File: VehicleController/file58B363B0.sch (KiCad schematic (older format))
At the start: 10 parts, among them P3 CONN_01X02, P4 MX150_8, U11 NDC7002N, U12 MCP2551

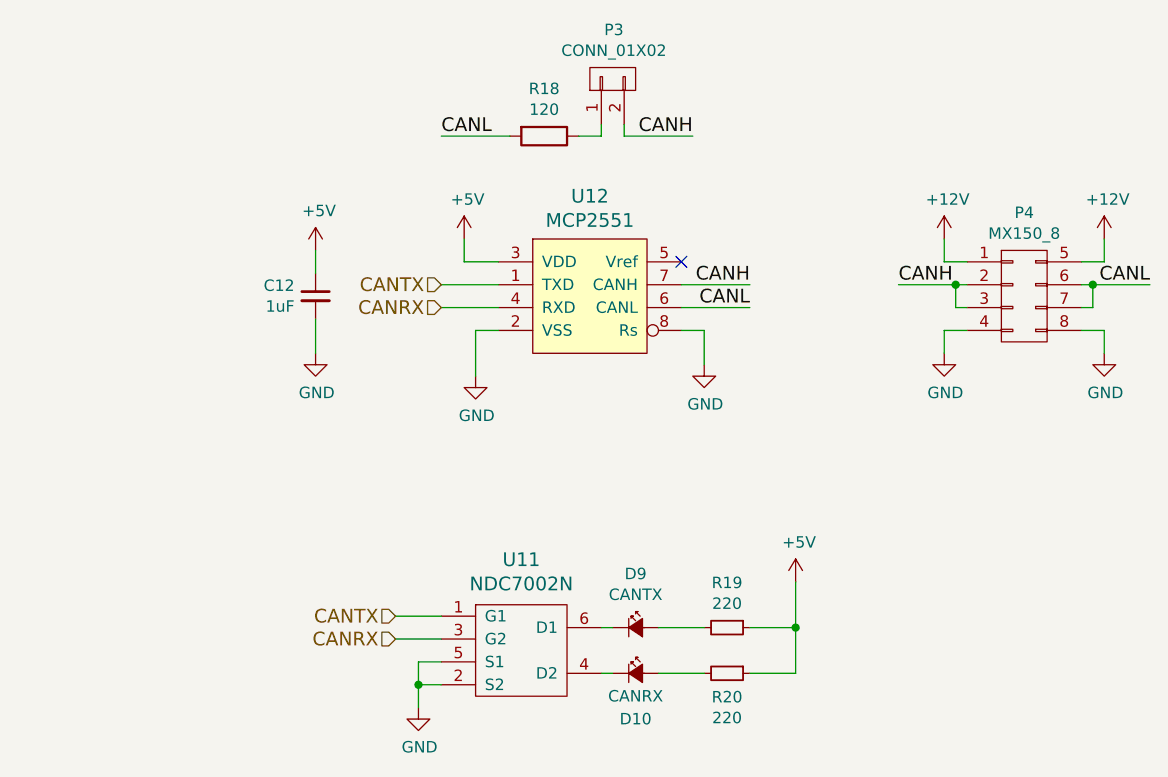
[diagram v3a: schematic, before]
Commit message: Add BTS4130's for 12v and 5v outputs
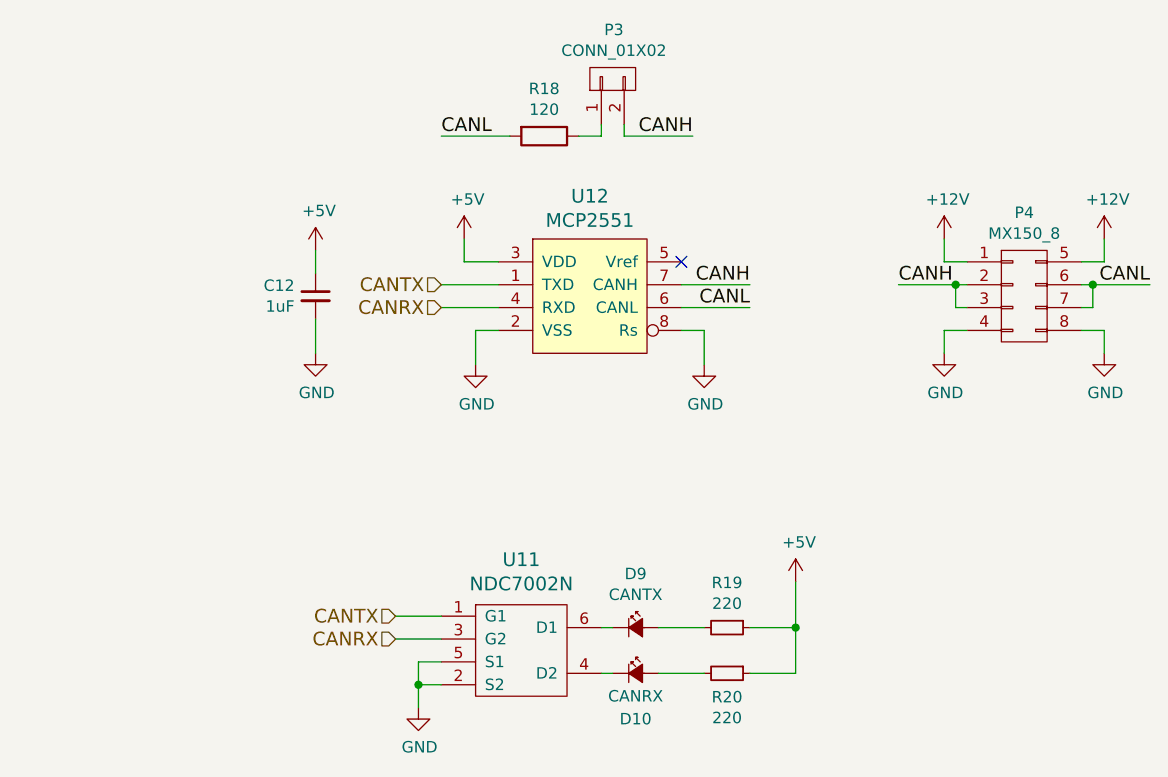
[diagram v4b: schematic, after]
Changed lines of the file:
@@
 L GND #PWR52
 U 1 1 58B3659A
-P 4950 3550
-F 0 "#PWR52" H 4950 3300 50  0001 C CNN
-F 1 "GND" H 4955 3377 50  0000 C CNN
-F 2 "" H 4950 3550 50  0000 C CNN
-F 3 "" H 4950 3550 50  0000 C CNN
-	1    4950 3550
+P 4950 3500
+F 0 "#PWR52" H 4950 3250 50  0001 C CNN
+F 1 "GND" H 4955 3327 50  0000 C CNN
+F 2 "" H 4950 3500 50  0000 C CNN
+F 3 "" H 4950 3500 50  0000 C CNN
+	1    4950 3500
 	1    0    0    -1
 $EndComp
@@
 	4900 3050 5050 3050
 Wire Wire Line
-	4950 3550 4950 3350
+	4950 3500 4950 3350
 Wire Wire Line
 	4950 3350 5050 3350
@@
 CANH
 Wire Wire Line
-	6800 3150 7100 3150
+	6800 3150 7050 3150
+Wire Wire Line
+	7050 3150 7100 3150
 Wire Wire Line
 	7100 3250 7050 3250
@@
 	7000 3350 7100 3350
 Wire Wire Line
-	7600 3150 7900 3150
+	7600 3150 7650 3150
+Wire Wire Line
+	7650 3150 7900 3150
 Text Label 7900 3150 2    60   ~ 0
 CANL
@@
 $EndComp
 Wire Wire Line
-	4700 4800 4700 5000
+	4700 4800 4700 4900
+Wire Wire Line
+	4700 4900 4700 5000
 Wire Wire Line
 	4700 4800 4800 4800
@@
 	6150 4650 6350 4650
 Wire Wire Line
-	6350 4450 6350 4850
+	6350 4450 6350 4650
+Wire Wire Line
+	6350 4650 6350 4850
 Wire Wire Line
 	6350 4850 6150 4850

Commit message: More updates prior to finalizing design
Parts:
- renumbered D9 to D11, D10 to D12, P3 to P4, P4 to P5, R18 to R32, R19 to R33, R20 to R34, U11 to U14, U12 to U15
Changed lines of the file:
@@
 $EndDescr
 $Comp
-L MCP2551 U12
+L MCP2551 U15
 U 1 1 58B36586
 P 5450 3250
-F 0 "U12" H 5450 3737 60  0000 C CNN
+F 0 "U15" H 5450 3737 60  0000 C CNN
 F 1 "MCP2551" H 5450 3631 60  0000 C CNN
 F 2 "SMD_Packages:SOIC-8-N" H 5450 3250 60  0001 C CNN
@@
 $EndComp
 $Comp
-L GND #PWR53
+L GND #PWR056
 U 1 1 58B3658D
 P 5950 3500
-F 0 "#PWR53" H 5950 3250 50  0001 C CNN
+F 0 "#PWR056" H 5950 3250 50  0001 C CNN
 F 1 "GND" H 5955 3327 50  0000 C CNN
 F 2 "" H 5950 3500 50  0000 C CNN
@@
 NoConn ~ 5850 3050
 $Comp
-L +5V #PWR51
+L +5V #PWR057
 U 1 1 58B36594
 P 4900 2950
-F 0 "#PWR51" H 4900 2800 50  0001 C CNN
+F 0 "#PWR057" H 4900 2800 50  0001 C CNN
 F 1 "+5V" H 4915 3123 50  0000 C CNN
 F 2 "" H 4900 2950 50  0000 C CNN
@@
 $EndComp
 $Comp
-L GND #PWR52
+L GND #PWR058
 U 1 1 58B3659A
 P 4950 3500
-F 0 "#PWR52" H 4950 3250 50  0001 C CNN
+F 0 "#PWR058" H 4950 3250 50  0001 C CNN
 F 1 "GND" H 4955 3327 50  0000 C CNN
 F 2 "" H 4950 3500 50  0000 C CNN
@@
 $EndComp
 $Comp
-L R R18
+L R R32
 U 1 1 58B365A2
 P 5250 2500
-F 0 "R18" V 5043 2500 50  0000 C CNN
+F 0 "R32" V 5043 2500 50  0000 C CNN
 F 1 "120" V 5134 2500 50  0000 C CNN
 F 2 "Resistors_SMD:R_0805_HandSoldering" V 5180 2500 50  0001 C CNN
@@
 CANL
 $Comp
-L CONN_01X02 P3
+L CONN_01X02 P4
 U 1 1 58B365AA
 P 5550 2250
-F 0 "P3" V 5765 2245 50  0000 C CNN
+F 0 "P4" V 5765 2245 50  0000 C CNN
 F 1 "CONN_01X02" V 5674 2245 50  0000 C CNN
 F 2 "Pin_Headers:Pin_Header_Angled_1x02" H 5550 2250 50  0001 C CNN
@@
 $EndComp
 $Comp
-L +5V #PWR48
+L +5V #PWR059
 U 1 1 58B0DEC8
 P 4250 3000
-F 0 "#PWR48" H 4250 2850 50  0001 C CNN
+F 0 "#PWR059" H 4250 2850 50  0001 C CNN
 F 1 "+5V" H 4265 3173 50  0000 C CNN
 F 2 "" H 4250 3000 50  0000 C CNN
@@
 $EndComp
 $Comp
-L GND #PWR49
+L GND #PWR060
 U 1 1 58B0DF2A
 P 4250 3450
-F 0 "#PWR49" H 4250 3200 50  0001 C CNN
+F 0 "#PWR060" H 4250 3200 50  0001 C CNN
 F 1 "GND" H 4255 3277 50  0000 C CNN
 F 2 "" H 4250 3450 50  0000 C CNN
@@
 	4250 3450 4250 3300
 $Comp
-L MX150_8 P4
+L MX150_8 P5
 U 1 1 58B7A4A8
 P 7350 3200
-F 0 "P4" H 7350 3565 50  0000 C CNN
+F 0 "P5" H 7350 3565 50  0000 C CNN
 F 1 "MX150_8" H 7350 3474 50  0000 C CNN
 F 2 "UNCAMotorsports:MX150_8Pin" H 7350 2000 50  0001 C CNN
@@
 CANH
 Wire Wire Line
-	6800 3150 7050 3150
-Wire Wire Line
-	7050 3150 7100 3150
+	6800 3150 7100 3150
 Wire Wire Line
 	7100 3250 7050 3250
@@
 	7000 3050 7100 3050
 $Comp
-L GND #PWR56
+L GND #PWR061
 U 1 1 58B7F609
 P 7000 3450
-F 0 "#PWR56" H 7000 3200 50  0001 C CNN
+F 0 "#PWR061" H 7000 3200 50  0001 C CNN
 F 1 "GND" H 7005 3277 50  0000 C CNN
 F 2 "" H 7000 3450 50  0000 C CNN
@@
 	7000 3350 7100 3350
 Wire Wire Line
-	7600 3150 7650 3150
-Wire Wire Line
-	7650 3150 7900 3150
+	7600 3150 7900 3150
 Text Label 7900 3150 2    60   ~ 0
 CANL
@@
 	7700 3050 7700 2950
 $Comp
-L GND #PWR58
+L GND #PWR062
 U 1 1 58B7FA08
 P 7700 3450
-F 0 "#PWR58" H 7700 3200 50  0001 C CNN
+F 0 "#PWR062" H 7700 3200 50  0001 C CNN
 F 1 "GND" H 7705 3277 50  0000 C CNN
 F 2 "" H 7700 3450 50  0000 C CNN
@@
 	7700 3350 7700 3450
 $Comp
-L +12V #PWR55
+L +12V #PWR063
 U 1 1 58BABA64
 P 7000 2950
-F 0 "#PWR55" H 7000 2800 50  0001 C CNN
+F 0 "#PWR063" H 7000 2800 50  0001 C CNN
 F 1 "+12V" H 7015 3123 50  0000 C CNN
 F 2 "" H 7000 2950 50  0000 C CNN
@@
 $EndComp
 $Comp
-L +12V #PWR57
+L +12V #PWR064
 U 1 1 58BABA85
 P 7700 2950
-F 0 "#PWR57" H 7700 2800 50  0001 C CNN
+F 0 "#PWR064" H 7700 2800 50  0001 C CNN
 F 1 "+12V" H 7715 3123 50  0000 C CNN
 F 2 "" H 7700 2950 50  0000 C CNN
@@
 $EndComp
 $Comp
-L NDC7002N U11
+L NDC7002N U14
 U 1 1 58C2C3D8
 P 5150 4750
-F 0 "U11" H 5150 5147 60  0000 C CNN
+F 0 "U14" H 5150 5147 60  0000 C CNN
 F 1 "NDC7002N" H 5150 5041 60  0000 C CNN
 F 2 "TO_SOT_Packages_SMD:SOT-23-6" H 1200 1900 60  0001 C CNN
@@
 	4600 4700 4800 4700
 $Comp
-L GND #PWR50
+L GND #PWR065
 U 1 1 58C2C777
 P 4700 5000
-F 0 "#PWR50" H 1200 2500 50  0001 C CNN
+F 0 "#PWR065" H 1200 2500 50  0001 C CNN
 F 1 "GND" H 4705 4827 50  0000 C CNN
 F 2 "" H 1200 2750 50  0001 C CNN
@@
 $EndComp
 Wire Wire Line
-	4700 4800 4700 4900
-Wire Wire Line
-	4700 4900 4700 5000
+	4700 4800 4700 5000
 Wire Wire Line
 	4700 4800 4800 4800
@@
 Connection ~ 4700 4900
 $Comp
-L LED_Small_ALT D9
+L LED_Small_ALT D11
 U 1 1 58C2C900
 P 5650 4650
-F 0 "D9" H 5650 4885 50  0000 C CNN
+F 0 "D11" H 5650 4885 50  0000 C CNN
 F 1 "CANTX" H 5650 4794 50  0000 C CNN
 F 2 "LEDs:LED-0805" V 1100 3550 50  0001 C CNN
@@
 $EndComp
 $Comp
-L LED_Small_ALT D10
+L LED_Small_ALT D12
 U 1 1 58C2C94C
 P 5650 4850
-F 0 "D10" H 5650 4650 50  0000 C CNN
+F 0 "D12" H 5650 4650 50  0000 C CNN
 F 1 "CANRX" H 5650 4750 50  0000 C CNN
 F 2 "LEDs:LED-0805" V 1100 3750 50  0001 C CNN
@@
 	5500 4850 5550 4850
 $Comp
-L R_Small R19
+L R_Small R33
 U 1 1 58C2D567
 P 6050 4650
-F 0 "R19" V 5854 4650 50  0000 C CNN
+F 0 "R33" V 5854 4650 50  0000 C CNN
 F 1 "220" V 5945 4650 50  0000 C CNN
 F 2 "Resistors_SMD:R_0805_HandSoldering" H 650 3100 50  0001 C CNN
@@
 $EndComp
 $Comp
-L R_Small R20
+L R_Small R34
 U 1 1 58C2D5C7
 P 6050 4850
-F 0 "R20" V 6154 4850 50  0000 C CNN
+F 0 "R34" V 6154 4850 50  0000 C CNN
 F 1 "220" V 6245 4850 50  0000 C CNN
 F 2 "Resistors_SMD:R_0805_HandSoldering" H 650 3300 50  0001 C CNN
@@
 	5750 4850 5950 4850
 $Comp
-L +5V #PWR54
+L +5V #PWR066
 U 1 1 58C2D6D1
 P 6350 4450
-F 0 "#PWR54" H 850 2600 50  0001 C CNN
+F 0 "#PWR066" H 850 2600 50  0001 C CNN
 F 1 "+5V" H 6365 4623 50  0000 C CNN
 F 2 "" H 850 2750 50  0001 C CNN
@@
 	6150 4650 6350 4650
 Wire Wire Line
-	6350 4450 6350 4650
-Wire Wire Line
-	6350 4650 6350 4850
+	6350 4450 6350 4850
 Wire Wire Line
 	6350 4850 6150 4850

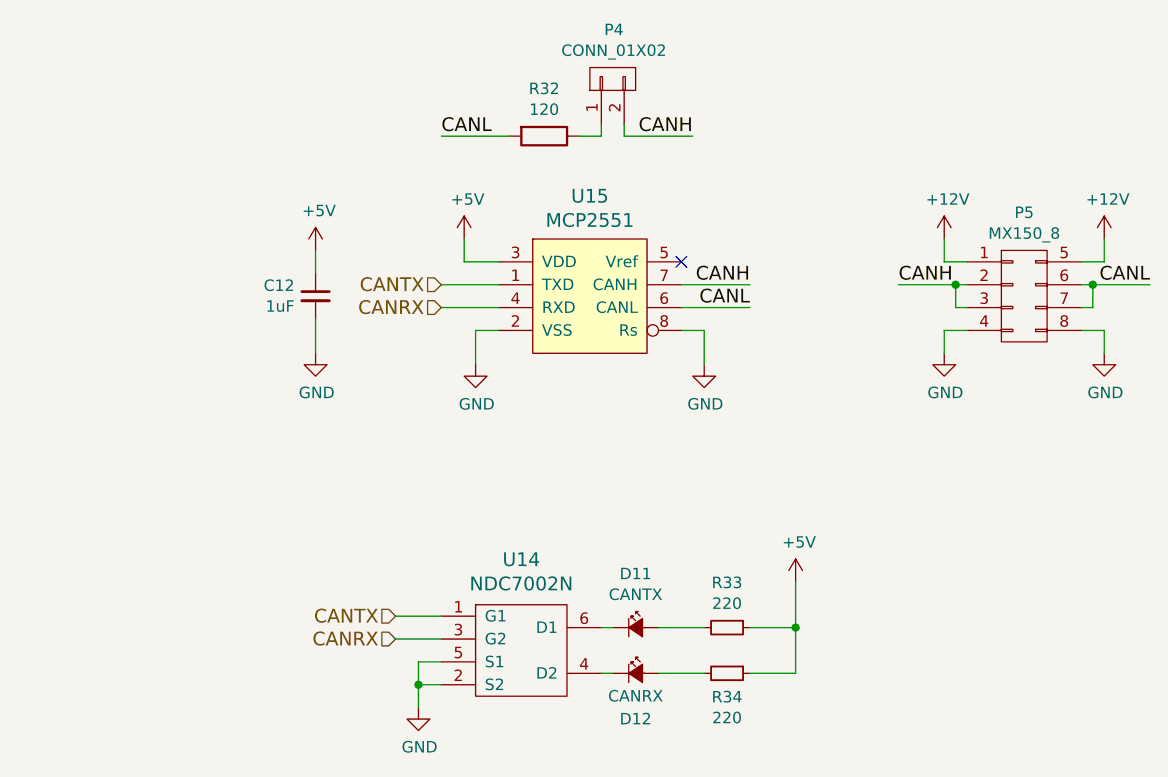
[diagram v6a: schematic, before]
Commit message: Fix Motor Controller Override circuit, better net names
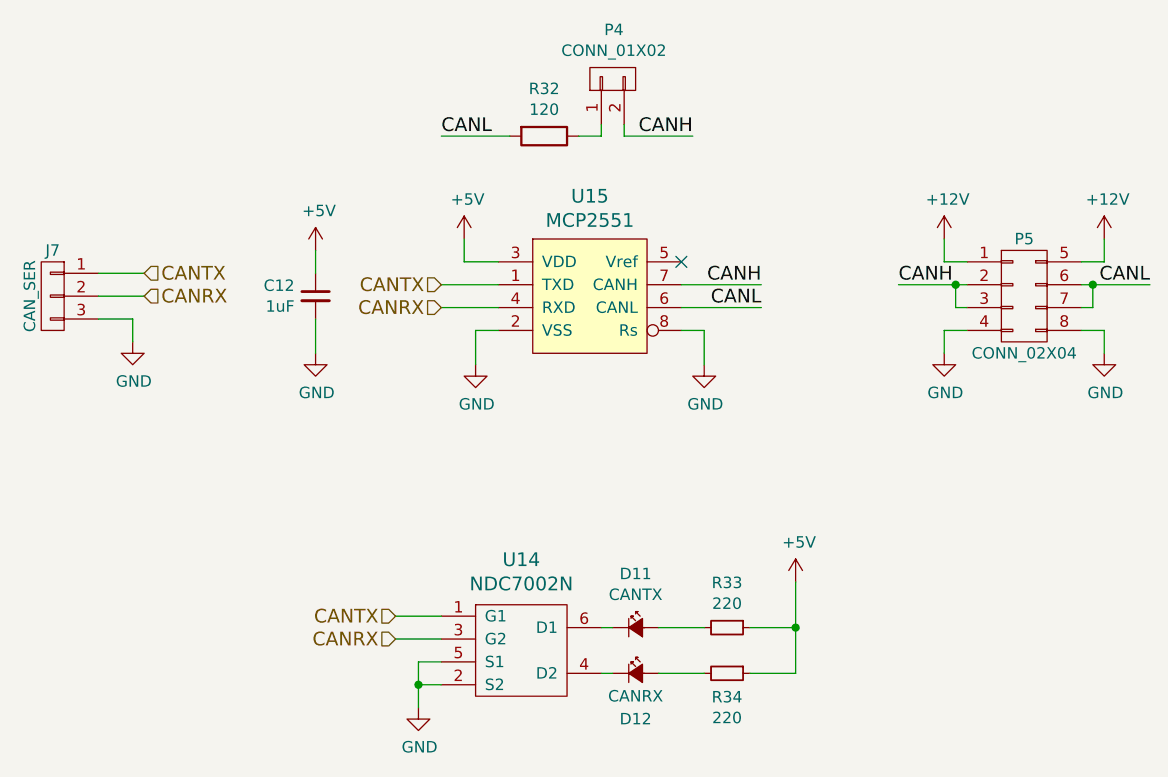
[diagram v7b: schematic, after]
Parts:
- removed P5: MX150_8, UNCAMotorsports:MX150_8Pin, symbol MX150_8
- added J7: CAN_SER, symbol CONN_01X03
- added P5: CONN_02X04, symbol CONN_02X04
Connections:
- net +12V: now also P5.1 (P1), P5.5 (P2)
- net CANH: now also P5.2 (P3), P5.3 (P5)
- net CANL: now also P5.6 (P4), P5.7 (P6)
- net CANRX: now also J7.2 (P2)
- net CANTX: now also J7.1 (P1)
- net GND: now also J7.3 (P3), P5.4 (P7), P5.8 (P8)
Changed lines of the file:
@@
 $EndComp
 $Comp
-L GND #PWR58
+L GND #PWR058
 U 1 1 58B3658D
 P 5950 3500
-F 0 "#PWR58" H 5950 3250 50  0001 C CNN
+F 0 "#PWR058" H 5950 3250 50  0001 C CNN
 F 1 "GND" H 5955 3327 50  0000 C CNN
 F 2 "" H 5950 3500 50  0000 C CNN
@@
 NoConn ~ 5850 3050
 $Comp
-L +5V #PWR56
+L +5V #PWR059
 U 1 1 58B36594
 P 4900 2950
-F 0 "#PWR56" H 4900 2800 50  0001 C CNN
+F 0 "#PWR059" H 4900 2800 50  0001 C CNN
 F 1 "+5V" H 4915 3123 50  0000 C CNN
 F 2 "" H 4900 2950 50  0000 C CNN
@@
 $EndComp
 $Comp
-L GND #PWR57
+L GND #PWR060
 U 1 1 58B3659A
 P 4950 3500
-F 0 "#PWR57" H 4950 3250 50  0001 C CNN
+F 0 "#PWR060" H 4950 3250 50  0001 C CNN
 F 1 "GND" H 4955 3327 50  0000 C CNN
 F 2 "" H 4950 3500 50  0000 C CNN
@@
 $EndComp
 $Comp
-L +5V #PWR53
+L +5V #PWR061
 U 1 1 58B0DEC8
 P 4250 3000
-F 0 "#PWR53" H 4250 2850 50  0001 C CNN
+F 0 "#PWR061" H 4250 2850 50  0001 C CNN
 F 1 "+5V" H 4265 3173 50  0000 C CNN
 F 2 "" H 4250 3000 50  0000 C CNN
@@
 $EndComp
 $Comp
-L GND #PWR54
+L GND #PWR062
 U 1 1 58B0DF2A
 P 4250 3450
-F 0 "#PWR54" H 4250 3200 50  0001 C CNN
+F 0 "#PWR062" H 4250 3200 50  0001 C CNN
 F 1 "GND" H 4255 3277 50  0000 C CNN
 F 2 "" H 4250 3450 50  0000 C CNN
@@
 Wire Wire Line
 	4250 3450 4250 3300
-$Comp
-L MX150_8 P5
-U 1 1 58B7A4A8
-P 7350 3200
-F 0 "P5" H 7350 3565 50  0000 C CNN
-F 1 "MX150_8" H 7350 3474 50  0000 C CNN
-F 2 "UNCAMotorsports:MX150_8Pin" H 7350 2000 50  0001 C CNN
-F 3 "" H 7350 2000 50  0000 C CNN
-	1    7350 3200
-	1    0    0    -1
-$EndComp
-Wire Wire Line
-	5850 3150 6150 3150
-Text Label 6150 3150 2    60   ~ 0
+Wire Wire Line
+	5850 3150 6200 3150
+Text Label 6200 3150 2    60   ~ 0
 CANH
-Text Label 6150 3250 2    60   ~ 0
+Text Label 6200 3250 2    60   ~ 0
 CANL
 Wire Wire Line
-	5850 3250 6150 3250
+	5850 3250 6200 3250
 Text Label 6800 3150 0    60   ~ 0
 CANH
@@
 	7000 3050 7100 3050
 $Comp
-L GND #PWR61
+L GND #PWR063
 U 1 1 58B7F609
 P 7000 3450
-F 0 "#PWR61" H 7000 3200 50  0001 C CNN
+F 0 "#PWR063" H 7000 3200 50  0001 C CNN
 F 1 "GND" H 7005 3277 50  0000 C CNN
 F 2 "" H 7000 3450 50  0000 C CNN
@@
 	7700 3050 7700 2950
 $Comp
-L GND #PWR63
+L GND #PWR064
 U 1 1 58B7FA08
 P 7700 3450
-F 0 "#PWR63" H 7700 3200 50  0001 C CNN
+F 0 "#PWR064" H 7700 3200 50  0001 C CNN
 F 1 "GND" H 7705 3277 50  0000 C CNN
 F 2 "" H 7700 3450 50  0000 C CNN
@@
 	7700 3350 7700 3450
 $Comp
-L +12V #PWR60
+L +12V #PWR065
 U 1 1 58BABA64
 P 7000 2950
-F 0 "#PWR60" H 7000 2800 50  0001 C CNN
+F 0 "#PWR065" H 7000 2800 50  0001 C CNN
 F 1 "+12V" H 7015 3123 50  0000 C CNN
 F 2 "" H 7000 2950 50  0000 C CNN
@@
 $EndComp
 $Comp
-L +12V #PWR62
+L +12V #PWR066
 U 1 1 58BABA85
 P 7700 2950
-F 0 "#PWR62" H 7700 2800 50  0001 C CNN
+F 0 "#PWR066" H 7700 2800 50  0001 C CNN
 F 1 "+12V" H 7715 3123 50  0000 C CNN
 F 2 "" H 7700 2950 50  0000 C CNN
@@
 	4600 4700 4800 4700
 $Comp
-L GND #PWR55
+L GND #PWR067
 U 1 1 58C2C777
 P 4700 5000
-F 0 "#PWR55" H 1200 2500 50  0001 C CNN
+F 0 "#PWR067" H 1200 2500 50  0001 C CNN
 F 1 "GND" H 4705 4827 50  0000 C CNN
 F 2 "" H 1200 2750 50  0001 C CNN
@@
 	5750 4850 5950 4850
 $Comp
-L +5V #PWR59
+L +5V #PWR068
 U 1 1 58C2D6D1
 P 6350 4450
-F 0 "#PWR59" H 850 2600 50  0001 C CNN
+F 0 "#PWR068" H 850 2600 50  0001 C CNN
 F 1 "+5V" H 6365 4623 50  0000 C CNN
 F 2 "" H 850 2750 50  0001 C CNN
@@
 	6350 4850 6150 4850
 Connection ~ 6350 4650
+$Comp
+L CONN_02X04 P5
+U 1 1 590C075D
+P 7350 3200
+F 0 "P5" H 7350 3450 50  0000 C CNN
+F 1 "CONN_02X04" H 7350 2950 50  0000 C CNN
+F 2 "" H 7350 2000 50  0001 C CNN
+F 3 "" H 7350 2000 50  0000 C CNN
+	1    7350 3200
+	1    0    0    -1
+$EndComp
+$Comp
+L CONN_01X03 J7
+U 1 1 590E71D7
+P 3100 3200
+F 0 "J7" H 3100 3400 50  0000 C CNN
+F 1 "CAN_SER" V 3200 3200 50  0000 C CNN
+F 2 "" H 3100 3200 50  0001 C CNN
+F 3 "" H 3100 3200 50  0001 C CNN
+	1    3100 3200
+	-1   0    0    -1
+$EndComp
+Text HLabel 3500 3100 2    60   Input ~ 0
+CANTX
+Text HLabel 3500 3200 2    60   Input ~ 0
+CANRX
+$Comp
+L GND #PWR069
+U 1 1 59121912
+P 3450 3400
+F 0 "#PWR069" H 3450 3150 50  0001 C CNN
+F 1 "GND" H 3455 3227 50  0000 C CNN
+F 2 "" H 3450 3400 50  0000 C CNN
+F 3 "" H 3450 3400 50  0000 C CNN
+	1    3450 3400
+	1    0    0    -1
+$EndComp
+Wire Wire Line
+	3300 3300 3450 3300
+Wire Wire Line
+	3450 3300 3450 3400
+Wire Wire Line
+	3300 3200 3500 3200
+Wire Wire Line
+	3300 3100 3500 3100
 $EndSCHEMATC
